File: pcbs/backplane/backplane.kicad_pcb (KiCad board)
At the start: 6 copper layers, 145 x 355 mm, 487 parts, among them J1 Conn_01x02, J10 AFBR-2624Z, J11 AFBR-2624Z, J12 AFBR-1624Z, J13 RJ45_Shielded, J14 Conn_01x02, J15 RJ45_Shielded, J16 RJ45_Shielded, J17 Conn_01x02, J18 RJ45_Shielded, J19 Conn_01x02, J2 Conn_02x15_Odd_Even, J20 RJ45_Shielded, J21 RJ45_Shielded, J22 Conn_01x02, J23 RJ45_Shielded, J24 Conn_01x02, J25 RJ45_Shielded, J26 RJ45_Shielded, J27 Conn_01x02, J28 RJ45_Shielded, J29 Conn_01x02, J3 Conn_02x20_Odd_Even, J30 RJ45_Shielded, J31 RJ45_Shielded, J32 Conn_01x02, J33 RJ45_Shielded, J34 Conn_01x02, J35 RJ45_Shielded, J36 RJ45_Shielded, J37 Conn_01x02, J38 RJ45_Shielded, J39 Conn_01x02, J4 RJ45_Shielded, J40 RJ45_Shielded, J41 RJ45_Shielded, J42 Conn_01x02, J43 RJ45_Shielded, J44 Conn_01x02, J45 RJ45_Shielded, J46 RJ45_Shielded, J47 Conn_01x02, J48 Conn_01x02, J5 AFBR-2624Z, J6 RJ45_Shielded, J7 RJ45_Shielded, J8 Conn_01x02, J9 AFBR-2624Z, Q1 MMBT3904, Q10 MMBT3906, Q11 MMBT3906, Q12 MMBT3904, Q13 MMBT3904, Q2 MMBT3904, Q3 MMBT3904, Q4 MMBT3904, Q5 MMBT3904, Q6 MMBT3904, Q7 MMBT3904, Q8 MMBT3904, Q9 D44H11G, U1 74LVC1G14, U10 74LVC2T45, U12 74LVC1G14, U13 74LVC2G02, U14 74LVC1G14, U15 74LVC2G02, U16 74LVC2G02, U17 74LVC1G14, U18 74LVC2G02, U19 74LVC1G14, U2 FIN1027, U20 74LVC2G02, U21 74LVC1G14, U22 74LVC2G02, U23 74LVC1G14, U24 74LVC2G02, U25 74LVC1G14, U26 74LVC2G02, U27 74LVC1G14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

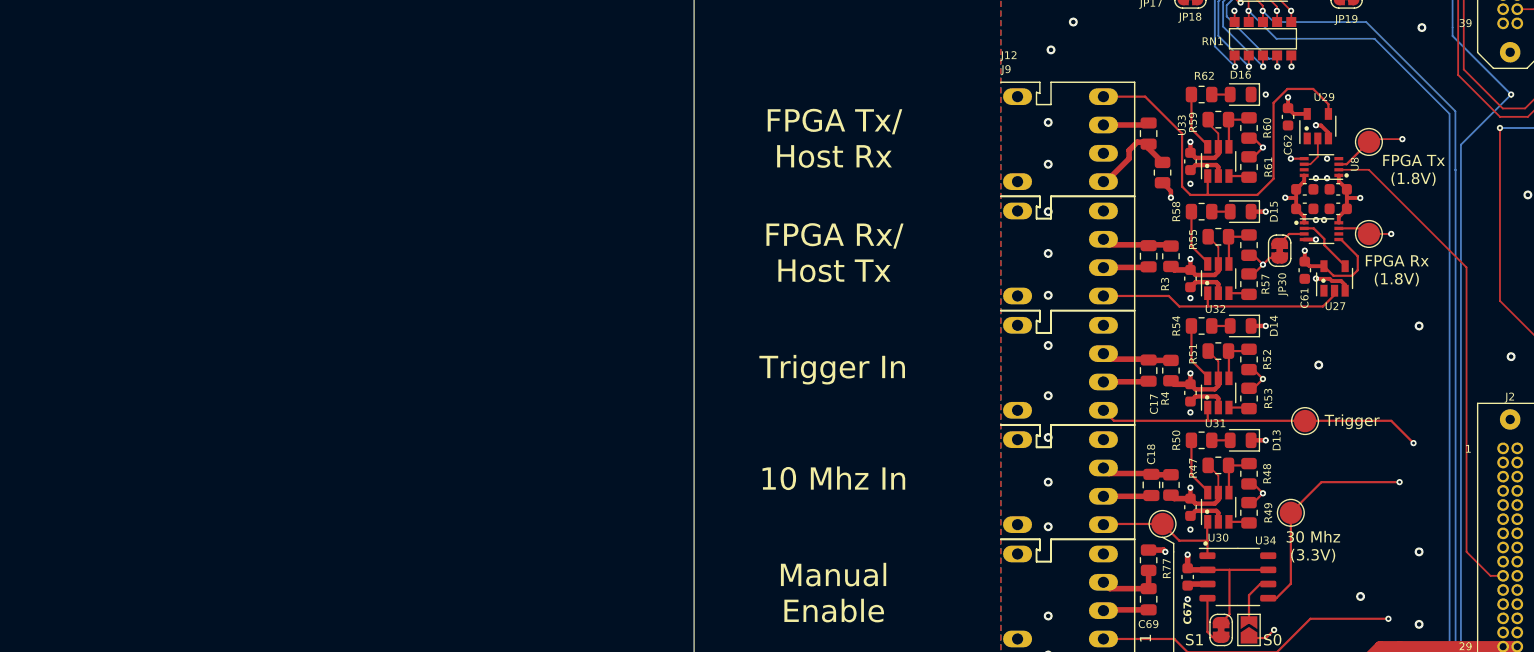
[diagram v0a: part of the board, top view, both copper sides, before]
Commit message: Backplane: changed timer ICs to TLC556 (fixes #45)
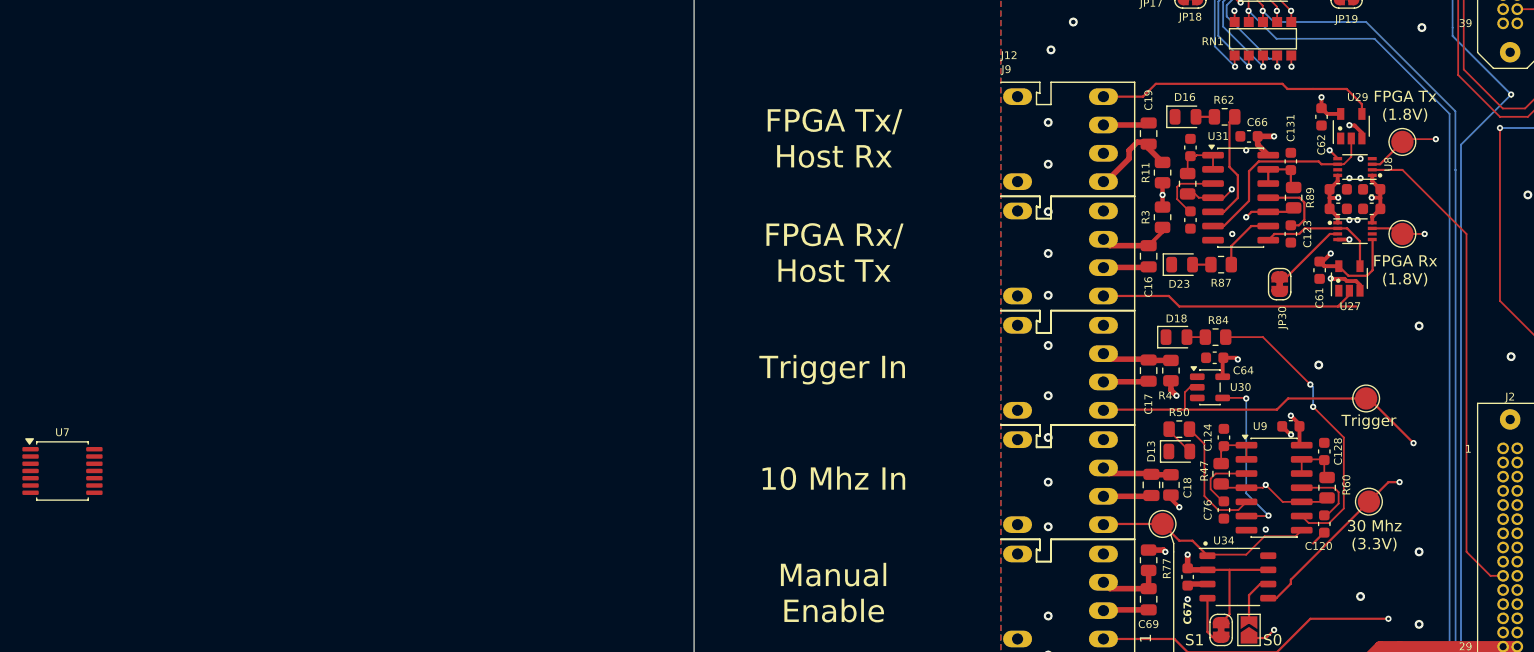
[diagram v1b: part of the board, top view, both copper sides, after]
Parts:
- removed C65: 100nF 50V X7R, Capacitor_SMD:C_0603_1608Metric
- removed D14, D15: Yellow, LED_SMD:LED_0805_2012Metric
- removed R48, R52, R56: 6.81K, Resistor_SMD:R_0805_2012Metric
- removed R49, R53, R57, R61: 180K, Resistor_SMD:R_0805_2012Metric
- removed R51, R55: 10K, Resistor_SMD:R_0805_2012Metric
- removed R54, R58: 1K, Resistor_SMD:R_0805_2012Metric
- removed U32, U33: LTC6993xS6-2, Package_TO_SOT_SMD:TSOT-23-6
- added C120: 100nF 50V X7R, Capacitor_SMD:C_0603_1608Metric, F.Cu at (84.0, 290.8)
- added C123: 100nF 50V X7R, Capacitor_SMD:C_0603_1608Metric, F.Cu at (81.0, 264.8)
- added C124: 100nF 50V X7R, Capacitor_SMD:C_0603_1608Metric, F.Cu at (75.0, 283.0)
- added C127: 100nF 50V X7R, Capacitor_SMD:C_0603_1608Metric, F.Cu at (72.0, 257.0)
- added C128: 100nF 50V X7R, Capacitor_SMD:C_0603_1608Metric, F.Cu at (84.0, 284.2)
- added C131: 100nF 50V X7R, Capacitor_SMD:C_0603_1608Metric, F.Cu at (81.0, 258.2)
- added C76: 100nF 50V X7R, Capacitor_SMD:C_0603_1608Metric, F.Cu at (75.0, 289.5)
- added C79: 100nF 50V X7R, Capacitor_SMD:C_0603_1608Metric, F.Cu at (72.0, 263.5)
- added D18: Yellow, LED_SMD:LED_0805_2012Metric, F.Cu at (70.8, 274.0)
- added D23: Yellow, LED_SMD:LED_0805_2012Metric, F.Cu at (71.2, 267.5)
- added R84: 1K, Resistor_SMD:R_0805_2012Metric, F.Cu at (74.2, 274.0)
- added R87: 1K, Resistor_SMD:R_0805_2012Metric, F.Cu at (74.8, 267.5)
- added R89: 4.7M, Resistor_SMD:R_0805_2012Metric, F.Cu at (81.2, 261.5)
- added U7: FIN1019MTC, Package_SO:TSSOP-14_4.4x5mm_P0.65mm, F.Cu at (-29.1, 286.0)
- added U9: TLC556, Package_SO:SOIC-14_3.9x8.7mm_P1.27mm, F.Cu at (79.5, 287.5)
- R47, R59: value 10K -> 4.7M
- R60: value 6.81K -> 4.7M
- U30: value LTC6993xS6-2 -> 74LVC1G14; footprint Package_TO_SOT_SMD:TSOT-23-6 -> Package_TO_SOT_SMD:SOT-23-5
- U31: value LTC6993xS6-2 -> TLC556; footprint Package_TO_SOT_SMD:TSOT-23-6 -> Package_SO:SOIC-14_3.9x8.7mm_P1.27mm
- moved R60 33.0 mm to (84.2, 287.5), turned to 90 degrees
- moved U31 17.6 mm to (76.5, 261.5), turned to 0 degrees
- moved C63 11.6 mm to (81.0, 282.0), turned to 0 degrees
- moved U30 10.8 mm to (73.8, 278.5), turned to 0 degrees
- moved TP12 7.07 mm to (88.0, 288.8)
- moved R59 6.37 mm to (71.8, 260.2), turned to 90 degrees
- moved TP27 5.84 mm to (87.8, 279.5)
- moved C66 5.71 mm to (77.2, 256.0), turned to 0 degrees
- moved D13 5.59 mm to (71.0, 284.2), turned to 0 degrees
- moved D16 5.33 mm to (71.6, 254.2), turned to 0 degrees
- moved C64 3.83 mm to (74.2, 275.9), turned to 0 degrees
- moved R3 3.58 mm to (69.5, 263.2), turned to -90 degrees
- moved C26 3.00 mm to (88.2, 260.8)
- moved C28 3.00 mm to (85.2, 260.8)
- moved C32 3.00 mm to (85.2, 262.5)
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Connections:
- net /Activitiy Indicator (Rx)/In renamed Net-(J9-Data_Out)
- net /Activity Indicator (Tx)/In renamed Net-(J12-Data_in)
- J10 pad 1: /Activity Indicator (Trigger)/In -> /FPGA Board, Signal Distribution/Trigger
- J11 pad 1: /Activity Indicator (10 Mhz)/In -> /Activity Indicator (Trigger & 10 Mhz)/In2
- JB2 pad 36: /Activity Indicator (Trigger)/In -> /FPGA Board, Signal Distribution/Trigger
- R47 pad 2: Net-(U30-DIV) -> Net-(U9A-DISCH)
- R50 pad 1: Net-(U30-OUT) -> Net-(U9A-OUT)
- R59 pad 2: Net-(U33-DIV) -> Net-(U31A-DISCH)
- R60 pad 1: Net-(U33-DIV) -> +3V3
- R60 pad 2: GND -> Net-(U9B-DISCH)
- R62 pad 1: Net-(U33-OUT) -> Net-(U31A-OUT)
- TP13 pad 1: /Activity Indicator (10 Mhz)/In -> /Activity Indicator (Trigger & 10 Mhz)/In2
- TP27 pad 1: /Activity Indicator (Trigger)/In -> /FPGA Board, Signal Distribution/Trigger
- U10 pad 2: /FPGA Board, Signal Distribution/UART_Rx_FPGA -> /Activity Indicator (Tx & Rx)/In2
- U27 pad 4: /FPGA Board, Signal Distribution/UART_Rx_FPGA -> /Activity Indicator (Tx & Rx)/In2
- U29 pad 2: /FPGA Board, Signal Distribution/UART_Tx_FPGA -> /Activity Indicator (Tx & Rx)/In1
- U30 pad 1: /Activity Indicator (10 Mhz)/In -> (no net)
- U30 pad 2: GND -> /FPGA Board, Signal Distribution/Trigger
- U30 pad 3: Net-(U30-SET) -> GND
- U30 pad 4: Net-(U30-DIV) -> /Activity Indicator (Trigger & 10 Mhz)/In1
- U31 pad 1: /Activity Indicator (Trigger)/In -> Net-(U31A-DISCH)
- U31 pad 2: GND -> Net-(U31A-DISCH)
- U31 pad 4: Net-(U31-DIV) -> +3V3
- U31 pad 5: +3V3 -> Net-(U31A-OUT)
- U31 pad 6: Net-(U31-OUT) -> /Activity Indicator (Tx & Rx)/In1
- U34 pad 1: /Activity Indicator (10 Mhz)/In -> /Activity Indicator (Trigger & 10 Mhz)/In2
- U8 pad 6: /FPGA Board, Signal Distribution/UART_Tx_FPGA -> /Activity Indicator (Tx & Rx)/In1
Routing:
- net /FPGA Board, Signal Distribution/Trigger: track 0.00 -> 80.2 mm, vias 0 -> 1
- net /Activity Indicator (Trigger)/In: track 77.6 -> 0.00 mm, vias 1 -> 0
- net GND: track 408.1 -> 377.9 mm, vias 400 -> 390
- net Net-(U9B-OUT): track 0.00 -> 26.3 mm, vias 0 -> 2
- net /Activity Indicator (Trigger & 10 Mhz)/In2: track 0.00 -> 19.9 mm
- net /Activity Indicator (Tx & Rx)/In1: track 0.00 -> 18.4 mm
- net /Activity Indicator (Trigger & 10 Mhz)/In1: track 0.00 -> 15.5 mm, vias 0 -> 2
- net /Activity Indicator (10 Mhz)/In: track 13.0 -> 0.00 mm
- net Net-(J12-Data_in): track 37.7 -> 25.3 mm
- net /Activity Indicator (Tx & Rx)/In2: track 0.00 -> 11.4 mm
- net Net-(U9A-OUT): track 0.00 -> 11.1 mm
- net Net-(U31A-OUT): track 0.00 -> 10.5 mm
- net Net-(U31B-CONT): track 0.00 -> 6.38 mm
- net Net-(U9B-CONT): track 0.00 -> 6.22 mm
- net Net-(U9A-CONT): track 0.00 -> 5.99 mm
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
